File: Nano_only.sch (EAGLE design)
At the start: 3 parts

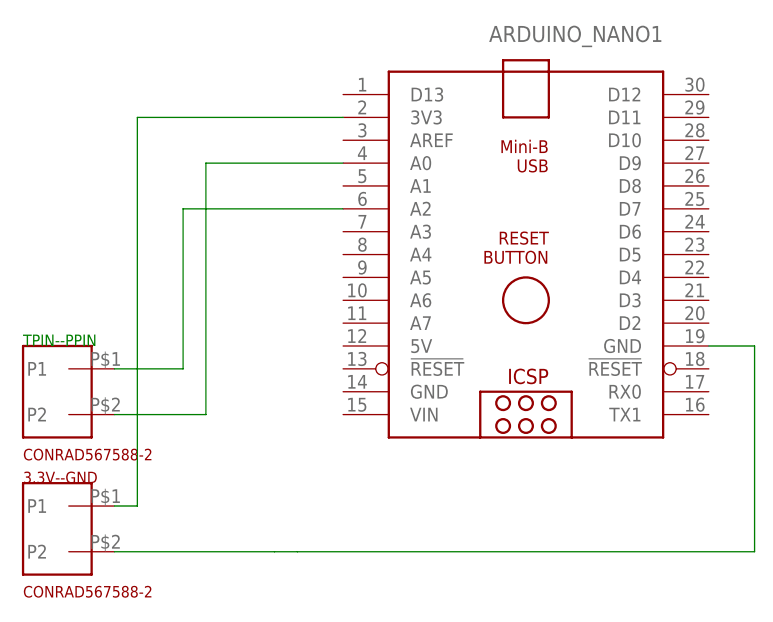
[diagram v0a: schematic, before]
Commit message: Added some text on Nano_only.brd
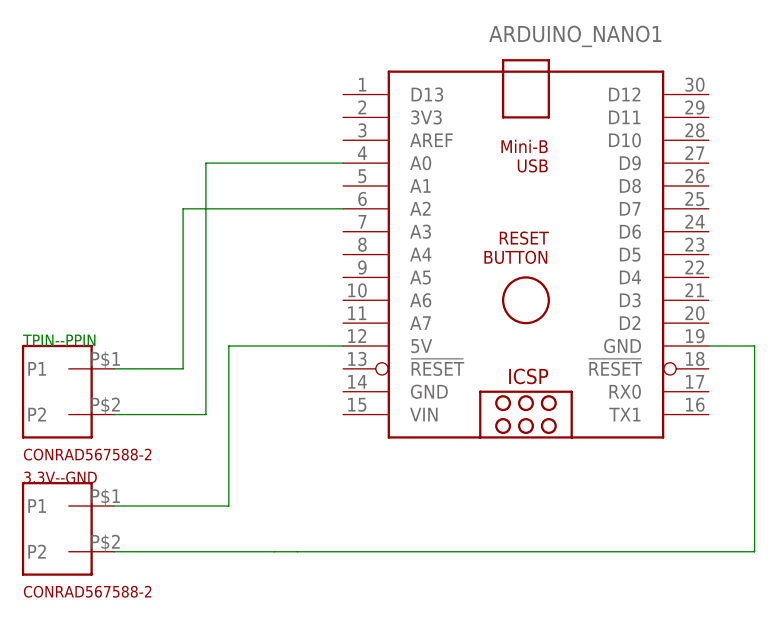
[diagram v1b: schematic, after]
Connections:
- removed net 3V3: 3.3V--GND.P1, ARDUINO_NANO1.3V3
- new net N$1: 3.3V--GND.P1, ARDUINO_NANO1.5V
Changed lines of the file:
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@@
 </segment>
 </net>
-<net name="3V3" class="0">
+<net name="N$1" class="0">
 <segment>
-<wire x1="-7.62" y1="83.82" x2="-7.62" y2="40.64" width="0.1524" layer="91"/>
 <pinref part="3.3V--GND" gate="G$1" pin="P1"/>
-<wire x1="-7.62" y1="40.64" x2="-10.16" y2="40.64" width="0.1524" layer="91"/>
-<wire x1="-7.62" y1="83.82" x2="15.24" y2="83.82" width="0.1524" layer="91"/>
-<pinref part="ARDUINO_NANO1" gate="G$1" pin="3V3"/>
+<wire x1="-10.16" y1="40.64" x2="2.54" y2="40.64" width="0.1524" layer="91"/>
+<pinref part="ARDUINO_NANO1" gate="G$1" pin="5V"/>
+<wire x1="2.54" y1="40.64" x2="2.54" y2="58.42" width="0.1524" layer="91"/>
+<wire x1="2.54" y1="58.42" x2="15.24" y2="58.42" width="0.1524" layer="91"/>
 </segment>
 </net>

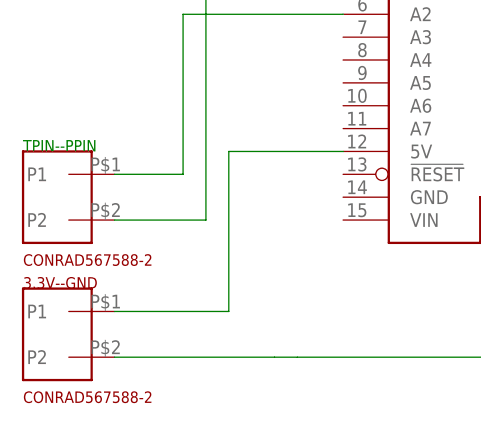
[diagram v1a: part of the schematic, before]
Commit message: few typos, 3V3 -> 5V
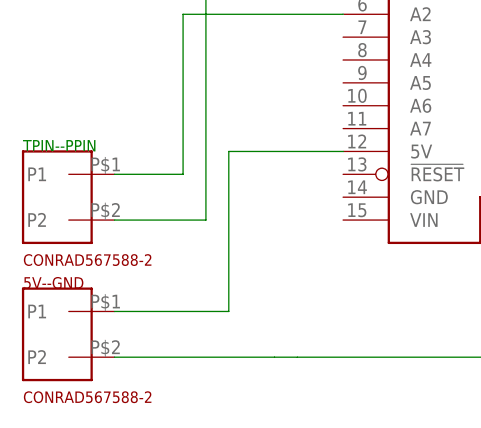
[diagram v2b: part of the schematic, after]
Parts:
- renumbered 3.3V--GND to 5V--GND
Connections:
- net N$1 renamed 5V
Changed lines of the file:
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@@
 </classes>
 <parts>
-<part name="3.3V--GND" library="johannes" deviceset="CONRAD567588-2" device=""/>
+<part name="5V--GND" library="johannes" deviceset="CONRAD567588-2" device=""/>
 <part name="TPIN--PPIN" library="johannes" deviceset="CONRAD567588-2" device=""/>
 <part name="ARDUINO_NANO1" library="ArduinoNanoV30" deviceset="ARDUINO_NANO" device=""/>
@@
 </plain>
 <instances>
-<instance part="3.3V--GND" gate="G$1" x="-15.24" y="38.1" smashed="yes" rot="R270">
+<instance part="5V--GND" gate="G$1" x="-15.24" y="38.1" smashed="yes" rot="R270">
 <attribute name="VALUE" x="-20.32" y="30.48" size="1.27" layer="94"/>
 <attribute name="NAME" x="-20.32" y="43.18" size="1.27" layer="94"/>
@@
 <net name="GND" class="0">
 <segment>
-<pinref part="3.3V--GND" gate="G$1" pin="P2"/>
+<pinref part="5V--GND" gate="G$1" pin="P2"/>
 <wire x1="-10.16" y1="35.56" x2="7.62" y2="35.56" width="0.1524" layer="91"/>
 <pinref part="ARDUINO_NANO1" gate="G$1" pin="GND@1"/>
@@
 </segment>
 </net>
-<net name="N$1" class="0">
+<net name="5V" class="0">
 <segment>
-<pinref part="3.3V--GND" gate="G$1" pin="P1"/>
+<pinref part="5V--GND" gate="G$1" pin="P1"/>
 <wire x1="-10.16" y1="40.64" x2="2.54" y2="40.64" width="0.1524" layer="91"/>
 <pinref part="ARDUINO_NANO1" gate="G$1" pin="5V"/>
